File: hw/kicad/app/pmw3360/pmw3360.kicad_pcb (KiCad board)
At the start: 2 copper layers, 45 x 45 mm, 2 parts, among them J2 TOP, J4 BUTTOM

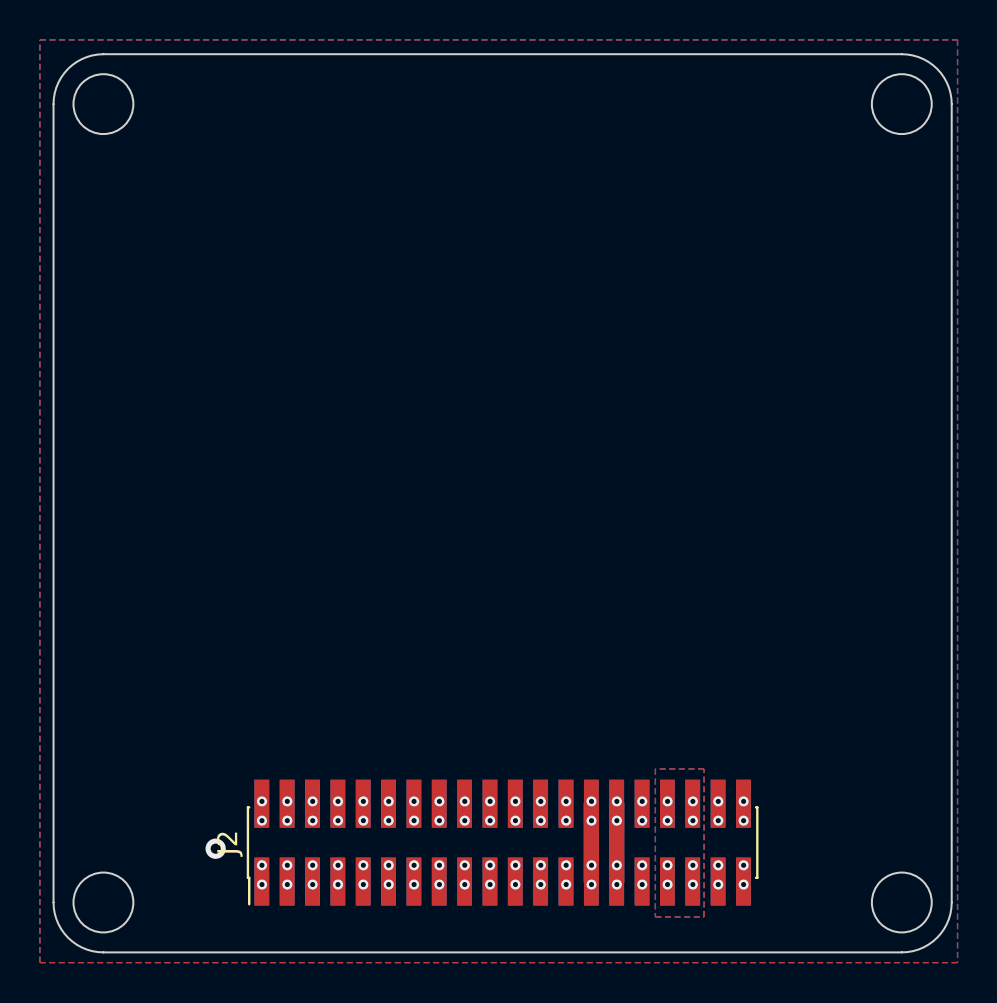
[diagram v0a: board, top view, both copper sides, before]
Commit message: 第二次打样的整改；dc motor改成了三路 io不够做不了四路；
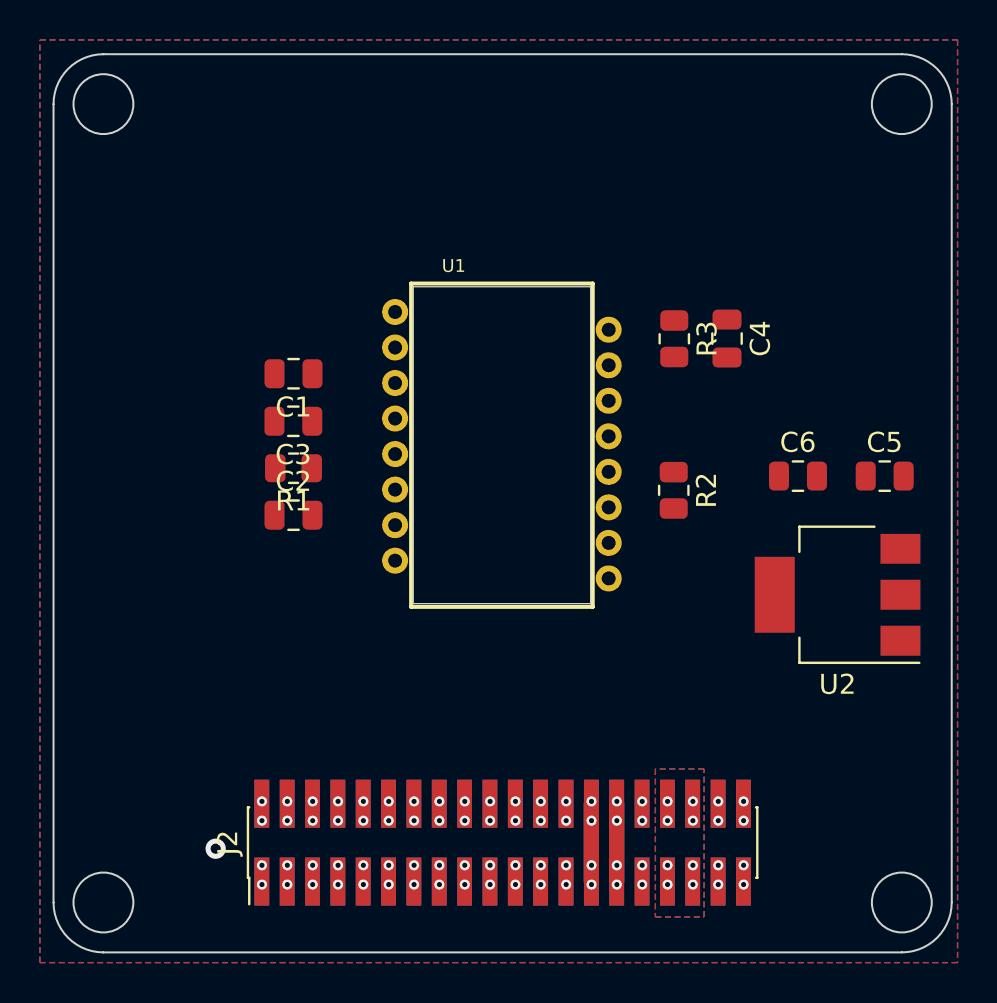
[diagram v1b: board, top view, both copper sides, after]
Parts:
- added C1: C, Capacitor_SMD:C_0805_2012Metric, F.Cu at (62.7, 48.7)
- added C2: 0.1uF, Capacitor_SMD:C_0805_2012Metric, F.Cu at (62.7, 55.8)
- added C3: 0.1uF, Capacitor_SMD:C_0805_2012Metric, F.Cu at (62.7, 51.1)
- added C4: 0.1uF, Capacitor_SMD:C_0805_2012Metric, F.Cu at (84.5, 47.0)
- added C5: 0.1uF, Capacitor_SMD:C_0805_2012Metric, F.Cu at (92.4, 53.9)
- added C6: 0.1uF, Capacitor_SMD:C_0805_2012Metric, F.Cu at (88.0, 53.9)
- added R1: 10k, Resistor_SMD:R_0805_2012Metric, F.Cu at (62.7, 53.5)
- added R2: 10k, Resistor_SMD:R_0805_2012Metric, F.Cu at (81.8, 54.6)
- added R3: 10k, Resistor_SMD:R_0805_2012Metric, F.Cu at (81.8, 47.0)
- added U1: PMW3360DM-T2QU, PMW3360:PMW3360DM, F.Cu at (73.2, 52.3)
- added U2: AMS1117-1.8, Package_TO_SOT_SMD:SOT-223-3_TabPin2, F.Cu at (90.0, 59.8)
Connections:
- net /+3.3V renamed +3.3V
- net /+5V renamed +5V
- net /GND renamed GND

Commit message: 新增app板 PMW3360
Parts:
- removed J4: BUTTOM, Connector_PinHeader_1.27mm:PinHeader_2x20_P1.27mm_Vertical_SMD
- removed R2: 10k, Resistor_SMD:R_0805_2012Metric
- added J1: TOP, Connector_PinHeader_1.27mm:PinHeader_2x20_P1.27mm_Vertical_SMD, F.Cu at (73.2, 72.2)
- J2: value TOP -> BUTTOM; moved to B.Cu
- moved C4 23.7 mm to (63.8, 58.7), turned to 0 degrees
- moved C2 21.0 mm to (82.4, 48.3), turned to 180 degrees
- moved C1 20.8 mm to (82.4, 55.6), turned to 0 degrees
- moved R3 20.3 mm to (63.8, 56.3), turned to 0 degrees
- moved R1 19.8 mm to (82.4, 50.6), turned to 0 degrees
- moved C3 19.8 mm to (82.4, 53.0), turned to 0 degrees
- moved C5 9.91 mm to (87.6, 62.6)
- moved U2 2.46 mm to (90.3, 57.4), turned to 0 degrees
- moved C6 1.99 mm to (87.6, 51.9), turned to 180 degrees
- moved U1 0.10 mm to (73.2, 52.2), turned to 180 degrees
- turned J2 to -90 degrees
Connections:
- C2 pad 1: Net-(C2-Pad1) -> GND
- C2 pad 2: GND -> Net-(U1-~{RESET})
- J2 pad 1: /ADC_1 -> /ADC_2
- J2 pad 10: /I2C_CLK -> /I2C_SDA
- J2 pad 11: /SPI_CS -> /SPI_CLK
- J2 pad 12: /SPI_CLK -> /SPI_CS
- J2 pad 13: /SPI_MOSI -> /SPI_MISO
- J2 pad 14: /SPI_MISO -> /SPI_MOSI
- J2 pad 15: /PWM_1 -> /GPIO_2
- J2 pad 16: /PWM_2 -> /GPIO_1
- J2 pad 17: /PWM_3 -> /GPIO_4
- J2 pad 18: /PWM_4 -> /GPIO_3
- J2 pad 19: /PWM_5 -> /GPIO_6
- J2 pad 2: /ADC_2 -> /ADC_1
- J2 pad 20: /PWM_6 -> /GPIO_5
- J2 pad 21: /PWM_7 -> /GPIO_8
- J2 pad 22: /PWM_8 -> /GPIO_7
- J2 pad 23: /CAN_H -> /GPIO_10
- J2 pad 24: /CAN_L -> /GPIO_9
- J2 pad 25: /USB+ -> /GPIO_12
- J2 pad 26: /USB- -> /GPIO_11
- J2 pad 3: /ADC_3 -> /ADC_4
- J2 pad 4: /ADC_4 -> /ADC_3
- J2 pad 5: /UART1_RX -> /UART1_Tx
- J2 pad 6: /UART1_TX -> /UART1_Rx
- J2 pad 7: /UART2_RX -> /UART2_Tx
- J2 pad 8: /UART2_TX -> /UART2_Rx
- J2 pad 9: /I2C_SDA -> /I2C_CLK
- R1 pad 1: +3.3V -> Net-(U1-~{RESET})
- R1 pad 2: Net-(C2-Pad1) -> +3.3V
- U1 pad 7: +3.3V -> Net-(U1-~{RESET})
- U1 pad 9: /CAN_L -> unconnected-(U1-MOTION-Pad9)
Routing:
- net +1V8: track 0.00 -> 58.1 mm
- net /SPI_CS: track 0.00 -> 28.4 mm
- net +3.3V: track 7.80 -> 35.8 mm
- net /SPI_MOSI: track 0.00 -> 26.9 mm
- net /SPI_CLK: track 0.00 -> 24.5 mm
- net /SPI_MISO: track 0.00 -> 21.0 mm
- net +5V: track 7.80 -> 23.5 mm
- net Net-(U1-~{RESET}): track 0.00 -> 5.26 mm
- net /LED: track 0.00 -> 3.17 mm
- net Net-(U1-VDDPIX): track 0.00 -> 2.88 mm
- net GND: vias 13 -> 20
- net /USB-: vias 2 -> 0
- net /USB+: vias 2 -> 0
- net /UART2_Tx: vias 0 -> 2
- net /UART2_TX: vias 2 -> 0
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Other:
- board text added: "Pindar v1.2 (App) PMW3360 v1.0"

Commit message: 更新打样资料
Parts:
- added C7: 4.7uF, Capacitor_SMD:C_1206_3216Metric, F.Cu at (82.6, 58.5)
- C1: value C -> 0.1uF
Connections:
- C4 pad 1: +1V8 -> +3.3V
- R3 pad 1: +1V8 -> +3.3V
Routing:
- net +1V8: track 58.1 -> 24.1 mm
- net +3.3V: track 35.8 -> 62.5 mm
- net Net-(U1-VDDPIX): track 2.88 -> 5.87 mm
